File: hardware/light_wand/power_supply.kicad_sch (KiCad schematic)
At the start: 13 parts, among them U1 TLV61070A

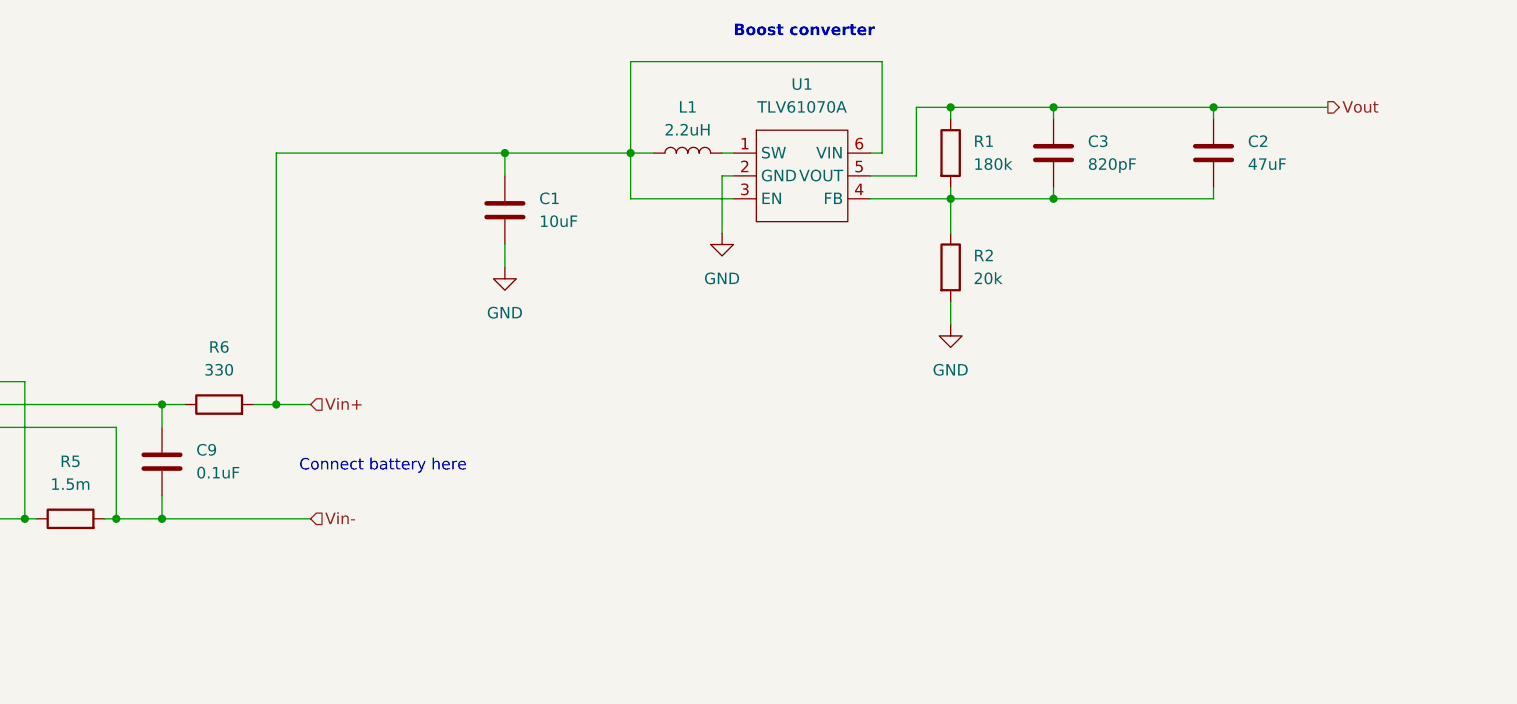
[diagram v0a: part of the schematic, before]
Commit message: Completed circuit schematic
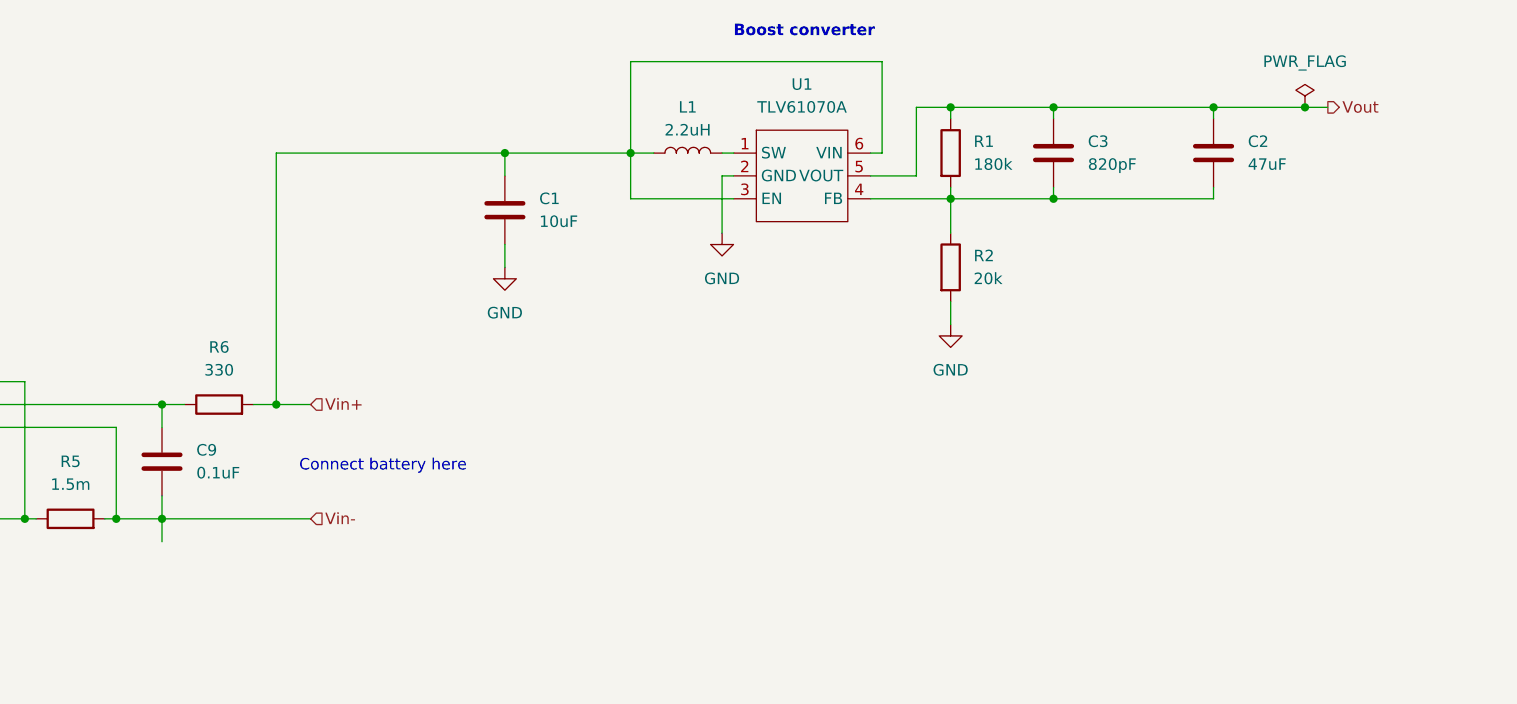
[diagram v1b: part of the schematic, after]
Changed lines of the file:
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@@
   (junction (at 187.96 55.88) (diameter 0) (color 0 0 0 0)
   )
+  (junction (at 227.33 55.88) (diameter 0) (color 0 0 0 0)
+  )
   (junction (at 217.17 55.88) (diameter 0) (color 0 0 0 0)
   )
@@
     (stroke (width 0) (type default))
   )
-  (wire (pts (xy 217.17 55.88) (xy 229.87 55.88))
+  (wire (pts (xy 217.17 55.88) (xy 227.33 55.88))
     (stroke (width 0) (type default))
   )
@@
     (stroke (width 0) (type default))
   )
+  (wire (pts (xy 100.33 104.14) (xy 100.33 101.6))
+    (stroke (width 0) (type default))
+  )
   (wire (pts (xy 199.39 66.04) (xy 217.17 66.04))
     (stroke (width 0) (type default))
@@
   )
   (wire (pts (xy 138.43 60.96) (xy 138.43 63.5))
+    (stroke (width 0) (type default))
+  )
+  (wire (pts (xy 227.33 55.88) (xy 229.87 55.88))
     (stroke (width 0) (type default))
   )
@@
         )
       )
+    )
+  )
+  (symbol (lib_id "power:PWR_FLAG") (at 227.33 55.88 0) (unit 1)
+    (in_bom yes) (on_board yes) (dnp no) (fields_autoplaced)
+    (property "Reference" "#FLG02" (at 227.33 53.975 0)
+      (effects (font (size 1.27 1.27)) hide)
+    )
+    (property "Value" "PWR_FLAG" (at 227.33 50.8 0)
+      (effects (font (size 1.27 1.27)))
+    )
+    (property "Footprint" "" (at 227.33 55.88 0)
+      (effects (font (size 1.27 1.27)) hide)
+    )
+    (property "Datasheet" "~" (at 227.33 55.88 0)
+      (effects (font (size 1.27 1.27)) hide)
+    )
+    (pin "1")
+    (instances
+      (project "light_wand"
+        (path "/1490551a-2c24-45df-b317-45d6c7f84af9/1ba98658-464e-4305-848f-5f718e928d99"
+          (reference "#FLG02") (unit 1)
+        )
+      )

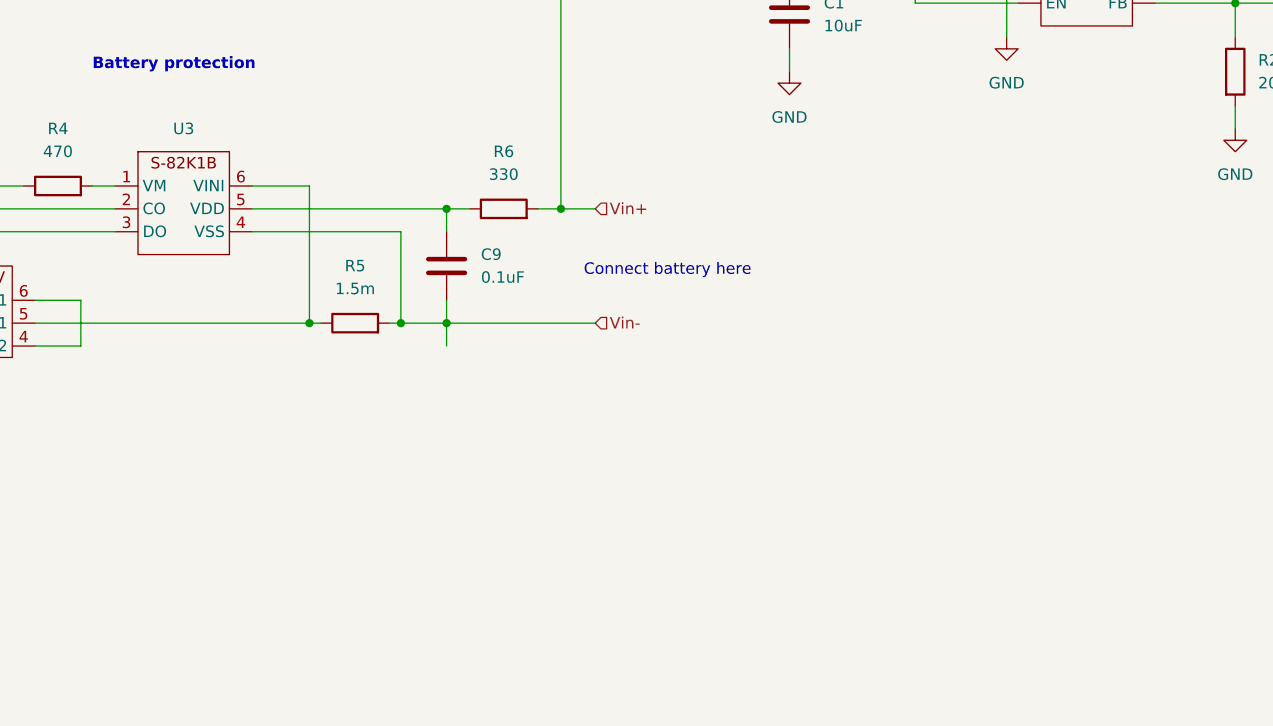
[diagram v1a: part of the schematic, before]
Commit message: Began laying out the PCB
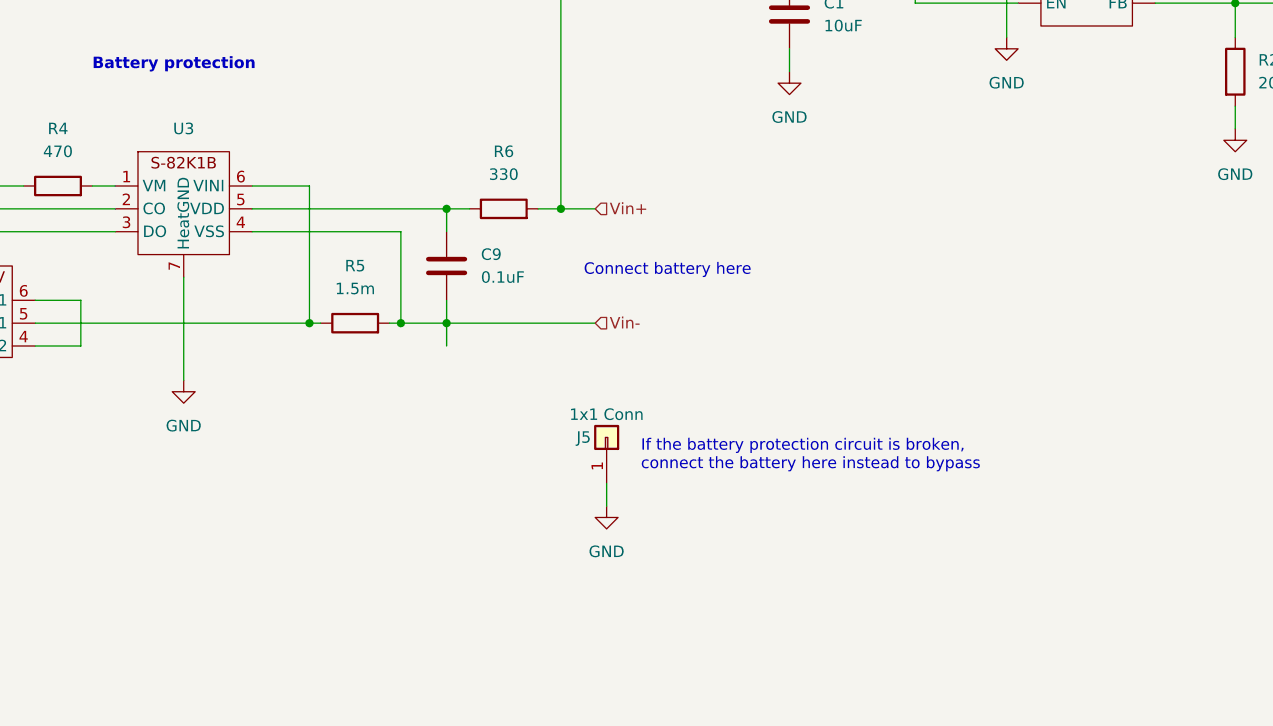
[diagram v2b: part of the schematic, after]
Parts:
- added J5: 1x1 Conn, Connector_Wire:SolderWire-0.5sqmm_1x01_D0.9mm_OD2.1mm, symbol Connector_Generic:Conn_01x01
- R1, R2, R4, R6: footprint Resistor_SMD:R_0201_0603Metric -> Resistor_SMD:R_0603_1608Metric
- U2: footprint Package_SO:TSOP-6_1.65x3.05mm_P0.95mm -> Package_TO_SOT_SMD:SOT-23-6_Handsoldering
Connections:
- net GND: now also U3.7 (HeatGND), J5.1 (Pin_1)
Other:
- note added: "If the battery protection circuit is broken, connect the battery here instead to bypass"

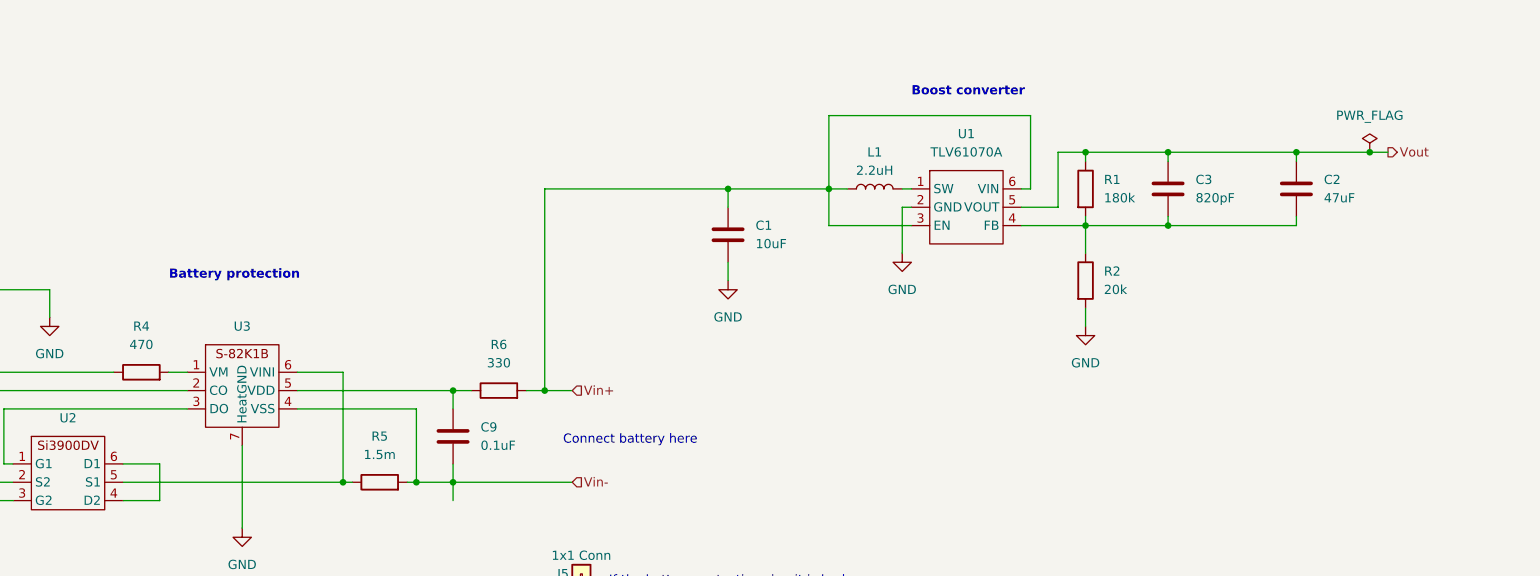
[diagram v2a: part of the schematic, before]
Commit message: Re-did schematic for new boost converter
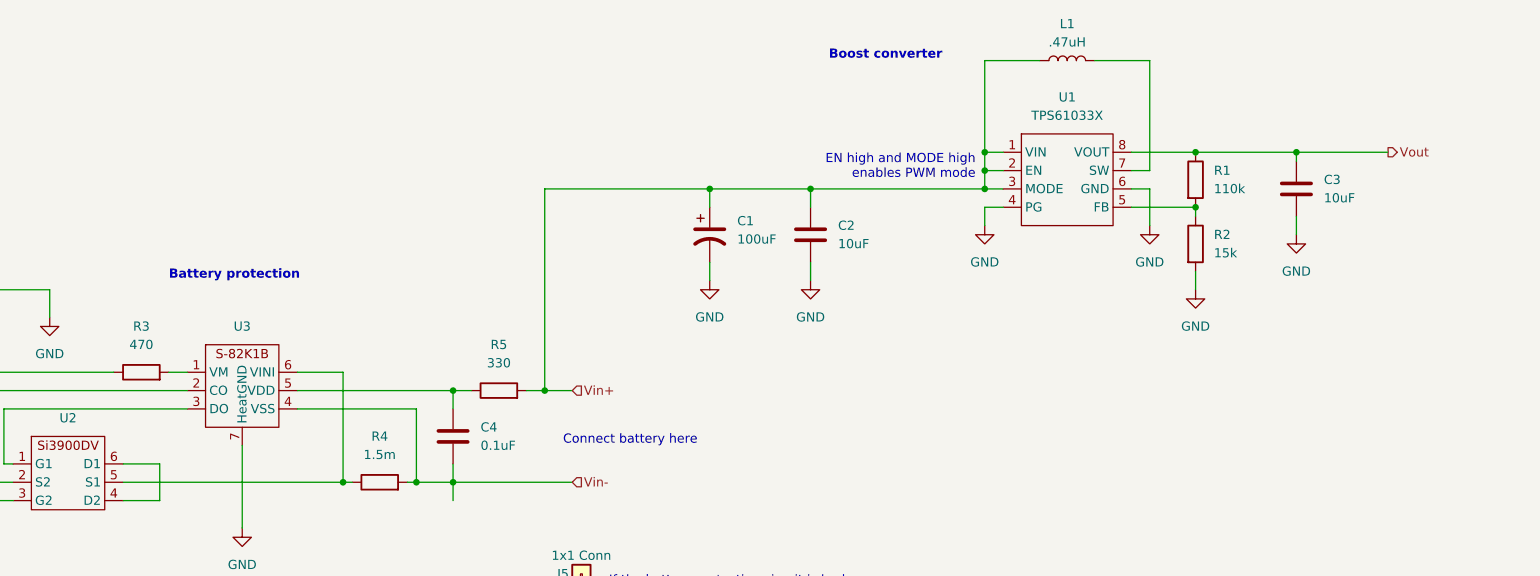
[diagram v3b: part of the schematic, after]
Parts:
- removed C3: 820pF, Capacitor_SMD:C_0603_1608Metric, symbol Device:C
- removed U1: TLV61070A, Package_TO_SOT_SMD:SOT-23-6_Handsoldering, symbol light_wand_library:TLV61070A
- added C1: 100uF, Capacitor_THT:CP_Radial_D5.0mm_P2.50mm, symbol Device:C_Polarized_US
- added U1: TPS61033X, Package_TO_SOT_SMD:SOT-583-8, symbol light_wand_library:TPS61033X
- C3: renamed from C2; value 47uF -> 10uF
- L1: value 2.2uH -> .47uH; footprint light_wand_footprints:74438357022_4.1x3.1mm_Inductor -> (none)
- R1: value 180k -> 110k; footprint Resistor_SMD:R_0603_1608Metric -> (none)
- R2: value 20k -> 15k; footprint Resistor_SMD:R_0603_1608Metric -> (none)
- renumbered C1 to C2, C9 to C4, R4 to R3, R5 to R4, R6 to R5
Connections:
- net GND: now also C3.2, C1.2, U1.4 (PG), U1.6 (GND)
- net Vin+: now also C1.1, U1.1 (VIN), U1.2 (EN), U1.3 (MODE)
- net Vout: now also U1.8 (VOUT)
- net at R1.2, R2.1: now also U1.5 (FB); no longer C3.2
- net at L1.2: now also U1.7 (SW)
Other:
- note added: "EN high and MODE high enables PWM mode"
- moved on the sheet: C2

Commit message: Pre updated PCB layout
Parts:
- L1: footprint (none) -> light_wand_footprints:Inductor_SMD_L_7.3x7.3_H3.5
- R1, R2: footprint (none) -> Resistor_SMD:R_0603_1608Metric
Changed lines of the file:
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@@
       (effects (font (size 1.27 1.27)) (justify left))
     )
-    (property "Footprint" "" (at 201.422 59.69 90)
+    (property "Footprint" "Resistor_SMD:R_0603_1608Metric" (at 201.422 59.69 90)
       (effects (font (size 1.27 1.27)) hide)
     )
@@
       (effects (font (size 1.27 1.27)))
     )
-    (property "Footprint" "" (at 185.42 43.18 0)
+    (property "Footprint" "light_wand_footprints:Inductor_SMD_L_7.3x7.3_H3.5" (at 185.42 43.18 0)
       (effects (font (size 1.27 1.27)) hide)
     )
@@
       (effects (font (size 1.27 1.27)) (justify left))
     )
-    (property "Footprint" "" (at 201.422 68.58 90)
+    (property "Footprint" "Resistor_SMD:R_0603_1608Metric" (at 201.422 68.58 90)
       (effects (font (size 1.27 1.27)) hide)
     )

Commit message: Completed PCB laout
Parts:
- added C5: 10uF, Capacitor_SMD:C_0603_1608Metric, symbol Device:C
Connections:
- net GND: now also C5.2
- net Vout: now also C5.1
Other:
- moved on the sheet: C3
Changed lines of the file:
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@@
   (junction (at 173.99 55.88) (diameter 0) (color 0 0 0 0)
   )
+  (junction (at 227.33 55.88) (diameter 0) (color 0 0 0 0)
+  )
+  (junction (at 215.9 55.88) (diameter 0) (color 0 0 0 0)
+  )
   (junction (at 203.2 63.5) (diameter 0) (color 0 0 0 0)
   )
@@
   (junction (at 149.86 60.96) (diameter 0) (color 0 0 0 0)
   )
-  (junction (at 217.17 55.88) (diameter 0) (color 0 0 0 0)
-  )
   (wire (pts (xy 173.99 43.18) (xy 181.61 43.18))
     (stroke (width 0) (type default))
@@
     (stroke (width 0) (type default))
   )
-  (wire (pts (xy 203.2 55.88) (xy 217.17 55.88))
+  (wire (pts (xy 203.2 55.88) (xy 215.9 55.88))
     (stroke (width 0) (type default))
   )
@@
     (stroke (width 0) (type default))
   )
-  (wire (pts (xy 217.17 55.88) (xy 217.17 57.15))
+  (wire (pts (xy 215.9 55.88) (xy 215.9 57.15))
     (stroke (width 0) (type default))
   )
@@
     (stroke (width 0) (type default))
   )
+  (wire (pts (xy 227.33 57.15) (xy 227.33 55.88))
+    (stroke (width 0) (type default))
+  )
+  (wire (pts (xy 215.9 55.88) (xy 227.33 55.88))
+    (stroke (width 0) (type default))
+  )
   (wire (pts (xy 33.02 104.14) (xy 39.37 104.14))
     (stroke (width 0) (type default))
@@
     (stroke (width 0) (type default))
   )
+  (wire (pts (xy 227.33 67.31) (xy 227.33 64.77))
+    (stroke (width 0) (type default))
+  )
   (wire (pts (xy 176.53 58.42) (xy 173.99 58.42))
     (stroke (width 0) (type default))
@@
     (stroke (width 0) (type default))
   )
-  (wire (pts (xy 217.17 55.88) (xy 229.87 55.88))
-    (stroke (width 0) (type default))
-  )
   (wire (pts (xy 39.37 101.6) (xy 35.56 101.6))
     (stroke (width 0) (type default))
@@
     (stroke (width 0) (type default))
   )
+  (wire (pts (xy 227.33 55.88) (xy 234.95 55.88))
+    (stroke (width 0) (type default))
+  )
   (wire (pts (xy 60.96 86.36) (xy 63.5 86.36))
     (stroke (width 0) (type default))
@@
     (stroke (width 0) (type default))
   )
-  (wire (pts (xy 217.17 67.31) (xy 217.17 64.77))
+  (wire (pts (xy 215.9 64.77) (xy 215.9 67.31))
     (stroke (width 0) (type default))
   )
@@
     (effects (font (size 1.27 1.27)) (justify left))
   )
-  (hierarchical_label "Vout" (shape output) (at 229.87 55.88 0) (fields_autoplaced)
+  (hierarchical_label "Vout" (shape output) (at 234.95 55.88 0) (fields_autoplaced)
     (effects (font (size 1.27 1.27)) (justify left))
   )
@@
     )
   )
-  (symbol (lib_id "Device:C") (at 217.17 60.96 0) (unit 1)
-    (in_bom yes) (on_board yes) (dnp no) (fields_autoplaced)
-    (property "Reference" "C3" (at 220.98 59.69 0)
-      (effects (font (size 1.27 1.27)) (justify left))
-    )
-    (property "Value" "10uF" (at 220.98 62.23 0)
-      (effects (font (size 1.27 1.27)) (justify left))
-    )
-    (property "Footprint" "Capacitor_SMD:C_0603_1608Metric" (at 218.1352 64.77 0)
-      (effects (font (size 1.27 1.27)) hide)
-    )
-    (property "Datasheet" "https://www.yuden.co.jp/productdata/catalog/mlcc06_e.pdf" (at 217.17 60.96 0)
+  (symbol (lib_id "Device:C") (at 215.9 60.96 0) (unit 1)
+    (in_bom yes) (on_board yes) (dnp no) (fields_autoplaced)
+    (property "Reference" "C3" (at 219.71 59.69 0)
+      (effects (font (size 1.27 1.27)) (justify left))
+    )
+    (property "Value" "10uF" (at 219.71 62.23 0)
+      (effects (font (size 1.27 1.27)) (justify left))
+    )
+    (property "Footprint" "Capacitor_SMD:C_0603_1608Metric" (at 216.8652 64.77 0)
+      (effects (font (size 1.27 1.27)) hide)
+    )
+    (property "Datasheet" "https://www.yuden.co.jp/productdata/catalog/mlcc06_e.pdf" (at 215.9 60.96 0)
       (effects (font (size 1.27 1.27)) hide)
     )
@@
     )
   )
-  (symbol (lib_id "power:GND") (at 217.17 67.31 0) (unit 1)
-    (in_bom yes) (on_board yes) (dnp no) (fields_autoplaced)
-    (property "Reference" "#PWR026" (at 217.17 73.66 0)
-      (effects (font (size 1.27 1.27)) hide)
-    )
-    (property "Value" "GND" (at 217.17 72.39 0)
-      (effects (font (size 1.27 1.27)))
-    )
-    (property "Footprint" "" (at 217.17 67.31 0)
-      (effects (font (size 1.27 1.27)) hide)
-    )
-    (property "Datasheet" "" (at 217.17 67.31 0)
+  (symbol (lib_id "power:GND") (at 215.9 67.31 0) (unit 1)
+    (in_bom yes) (on_board yes) (dnp no) (fields_autoplaced)
+    (property "Reference" "#PWR026" (at 215.9 73.66 0)
+      (effects (font (size 1.27 1.27)) hide)
+    )
+    (property "Value" "GND" (at 215.9 72.39 0)
+      (effects (font (size 1.27 1.27)))
+    )
+    (property "Footprint" "" (at 215.9 67.31 0)
+      (effects (font (size 1.27 1.27)) hide)
+    )
+    (property "Datasheet" "" (at 215.9 67.31 0)
       (effects (font (size 1.27 1.27)) hide)
     )
@@
         (path "/1490551a-2c24-45df-b317-45d6c7f84af9/1ba98658-464e-4305-848f-5f718e928d99"
           (reference "C1") (unit 1)
+        )
+      )
+    )
+  )
+  (symbol (lib_id "Device:C") (at 227.33 60.96 0) (unit 1)
+    (in_bom yes) (on_board yes) (dnp no) (fields_autoplaced)
+    (property "Reference" "C5" (at 231.14 59.69 0)
+      (effects (font (size 1.27 1.27)) (justify left))
+    )
+    (property "Value" "10uF" (at 231.14 62.23 0)
+      (effects (font (size 1.27 1.27)) (justify left))
+    )
+    (property "Footprint" "Capacitor_SMD:C_0603_1608Metric" (at 228.2952 64.77 0)
+      (effects (font (size 1.27 1.27)) hide)
+    )
+    (property "Datasheet" "https://www.yuden.co.jp/productdata/catalog/mlcc06_e.pdf" (at 227.33 60.96 0)
+      (effects (font (size 1.27 1.27)) hide)
+    )
+    (pin "1")
+    (pin "2")
+    (instances
+      (project "light_wand"
+        (path "/1490551a-2c24-45df-b317-45d6c7f84af9/1ba98658-464e-4305-848f-5f718e928d99"
+          (reference "C5") (unit 1)
         )
       )
@@
         )
       )
+    )
+  )
+  (symbol (lib_id "power:GND") (at 227.33 67.31 0) (unit 1)
+    (in_bom yes) (on_board yes) (dnp no) (fields_autoplaced)
+    (property "Reference" "#PWR027" (at 227.33 73.66 0)
+      (effects (font (size 1.27 1.27)) hide)
+    )
+    (property "Value" "GND" (at 227.33 72.39 0)
+      (effects (font (size 1.27 1.27)))
+    )
+    (property "Footprint" "" (at 227.33 67.31 0)
+      (effects (font (size 1.27 1.27)) hide)
+    )
+    (property "Datasheet" "" (at 227.33 67.31 0)
+      (effects (font (size 1.27 1.27)) hide)
+    )
+    (pin "1")
+    (instances
+      (project "light_wand"
+        (path "/1490551a-2c24-45df-b317-45d6c7f84af9/1ba98658-464e-4305-848f-5f718e928d99"
+          (reference "#PWR027") (unit 1)
+        )
+      )
